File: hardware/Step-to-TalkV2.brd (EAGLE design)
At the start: 20.5 x 24.5 mm, 19 parts, among them J1 Pogo Pad, J2 Pogo Pad, J3 Pogo Pad, J4 Pogo Pad, J5 Pogo Pad, J6 Pogo Pad, U1 ATTINY85

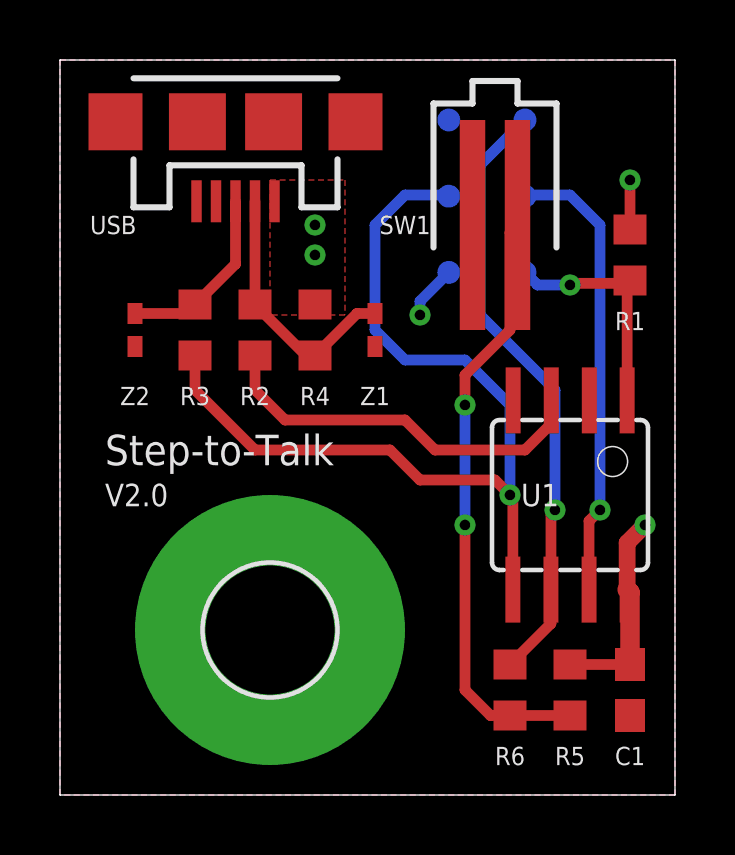
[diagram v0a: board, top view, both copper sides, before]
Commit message: Optimize routing, increase diode pad size.
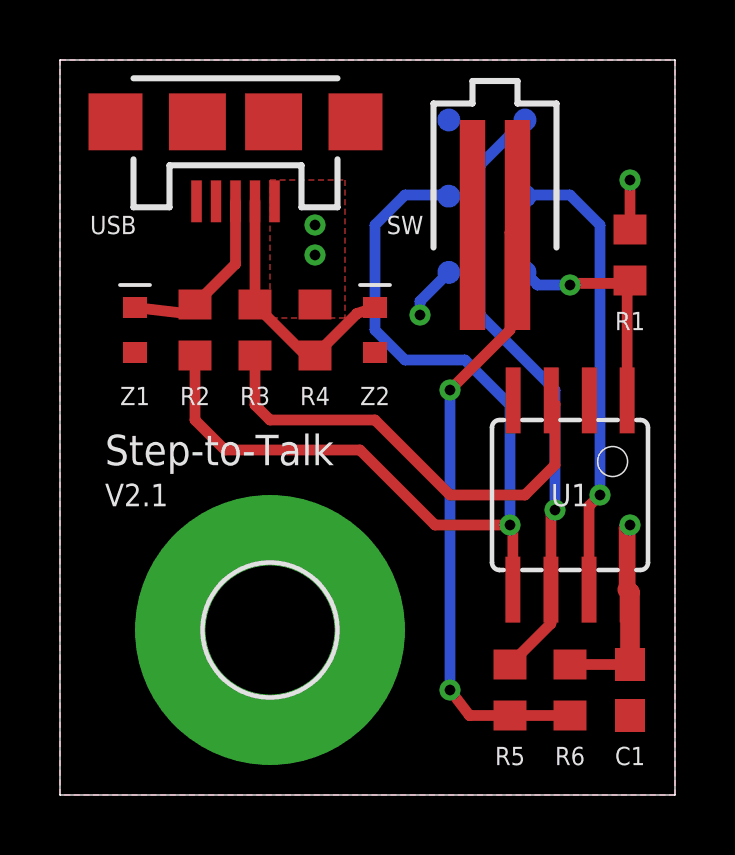
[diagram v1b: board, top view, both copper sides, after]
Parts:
- R5: value 10KΩ -> 200Ω
- R6: value 200Ω -> 10KΩ
- Z1, Z2: device NXP_60_26022015:SOD523 -> gjennings:SOD523-ENLARGED
- moved Z1 8.00 mm to (3.00, 16.0)
- moved Z2 8.00 mm to (11.0, 16.0)
- moved R2 2.00 mm to (5.00, 16.0)
- moved R3 2.00 mm to (7.00, 16.0)
- moved R5 2.00 mm to (15.5, 4.00), turned to 270 degrees
- moved R6 2.00 mm to (17.5, 4.00), turned to 90 degrees
- renumbered SW1 to SW
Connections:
- net D+: now also R2.2, Z1.1; no longer R3.2, Z2.1
- net D-: now also R3.2, Z2.1; no longer R2.2, Z1.1
- net MISO: now also R5.1; no longer R6.1
- net MOSI: now also R2.1; no longer R3.1
- net N$2: now also R3.1; no longer R2.1
- net N$4: now also R5.2, R6.1; no longer R5.1, R6.2
- net VCC: now also R6.2; no longer R5.2
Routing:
- net N$2: track 13.0 -> 15.5 mm
- net MOSI: track 31.2 -> 32.2 mm
- net N$4: track 20.1 -> 20.9 mm
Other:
- board text added: "V2.1"
- board text removed: "V2.0"
